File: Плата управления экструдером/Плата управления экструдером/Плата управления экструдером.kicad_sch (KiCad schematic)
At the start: 23 parts, among them J1 USB_C_Receptacle_USB2.0_16P, J2 Conn_01x02_Pin, J3 Conn_01x02_Pin, J4 Conn_01x02_Pin, U1 ATmega328P-A, U3 CH340N, Y1 Crystal

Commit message: Плата управления_обновл
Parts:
- added Q1, Q2, Q3, Q4, Q5: IRLB8721, Package_TO_SOT_THT:TO-220-3_Vertical, symbol Transistor_FET:Q_NMOS_GDS
- added bl_touch: Conn_01x05_Pin, symbol Connector:Conn_01x05_Pin
- added cooler_mod, cooler_mod1, fan, heater, switch, term: Conn_01x02_Pin, Connector_JST:JST_XH_B2B-XH-A_1x02_P2.50mm_Vertical, symbol Connector:Conn_01x02_Pin
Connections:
- net GND: now also Q1.3 (S), Q2.3 (S), Q3.3 (S), Q4.3 (S), Q5.3 (S)
- new net: Q5.2 (D), switch.2 (Pin_2)
- new net: Q3.2 (D), heater.2 (Pin_2)
- new net: Q1.2 (D), fan.2 (Pin_2)
- new net: cooler_mod.2 (Pin_2), cooler_mod1.1 (Pin_1)
- new net: Q4.2 (D), term.2 (Pin_2)
- new net +24V: Q2.2 (D), cooler_mod.1 (Pin_1), cooler_mod1.2 (Pin_2), fan.1 (Pin_1), heater.1 (Pin_1), switch.1 (Pin_1), term.1 (Pin_1)
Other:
- moved on the sheet: R3

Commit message: разводка платы
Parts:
- removed Q4, Q5: IRLB8721, Package_TO_SOT_THT:TO-220-3_Vertical, symbol Transistor_FET:Q_NMOS_GDS
- added C11: 0.1 uF, Capacitor_SMD:C_0805_2012Metric_Pad1.18x1.45mm_HandSolder, symbol Device:C
- added R4, R5, R6: 10k, Resistor_SMD:R_0805_2012Metric_Pad1.20x1.40mm_HandSolder, symbol Device:R
- added R7: 4.7k, Resistor_SMD:R_0805_2012Metric_Pad1.20x1.40mm_HandSolder, symbol Device:R
- C4: value 0.1 мкФ -> 0.1 uF
- renumbered POWER_IN_24V to POWER_IN_24V1, bl_touch to bl_touch1, cooler_mod to cooler_mod2, extruder to extruder1, fan to fan1, heater to heater1, switch to switch1, term to term1
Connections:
- net +24V: no longer switch1.1 (Pin_1), term1.1 (Pin_1)
- net +5V: now also bl_touch1.2 (Pin_2), R7.1
- net GND: now also bl_touch1.1 (Pin_1), bl_touch1.4 (Pin_4), switch1.2 (Pin_2), term1.2 (Pin_2), C11.2, R4.2, R5.2, R6.2
- net heater: now reaches Q3.1 (G)
- net heater: now also U1.26 (PC3), R6.1
- net fan_control: now reaches Q1.1 (G)
- net fan_control: now also U1.27 (PC4), R5.1
- net switch: now reaches U1.12 (PB0)
- net switch: now also switch1.1 (Pin_1)
- net BL_Z-min: now reaches U1.13 (PB1)
- net BL_Z-min: now also bl_touch1.5 (Pin_5)
- net termistor: now reaches U1.23 (PC0)
- net termistor: now also term1.1 (Pin_1), C11.1, R7.2
- net BL_contr_signal: now reaches U1.24 (PC1)
- net BL_contr_signal: now also bl_touch1.3 (Pin_3)
- net cooler: now reaches U1.28 (PC5)
- net cooler: now also Q2.1 (G), R4.1
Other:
- moved on the sheet: bl_touch1, switch1

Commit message: Плата управления раздел
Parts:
- added H1, H2, H3, H4: MountingHole, MountingHole:MountingHole_3.2mm_M3, symbol Mechanical:MountingHole
- Y1: footprint Crystal:Crystal_HC49-U_Vertical -> Crystal:Crystal_SMD_HC49-SD_HandSoldering

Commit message: Коннекторы
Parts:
- added J5, J6, J7, J8: Conn_01x08_Pin, Connector_PinSocket_2.54mm:PinSocket_1x08_P2.54mm_Vertical, symbol Connector:Conn_01x08_Pin
- Y1: footprint Crystal:Crystal_SMD_HC49-SD_HandSoldering -> Crystal:Crystal_HC49-4H_Vertical
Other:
- moved on the sheet: A1, C3, J2, J3, J4, POWER_IN_24V1, extruder1

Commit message: Правка платы
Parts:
- removed J2, J3, J4: Conn_01x02_Pin, symbol Connector:Conn_01x02_Pin
- removed cooler_mod2: Conn_01x02_Pin, Connector_JST:JST_XH_B2B-XH-A_1x02_P2.50mm_Vertical, symbol Connector:Conn_01x02_Pin
- added J9: Conn_02x03_Odd_Even, Connector_PinHeader_2.54mm:PinHeader_2x03_P2.54mm_Vertical, symbol Connector_Generic:Conn_02x03_Odd_Even
- J7, J8: footprint Connector_PinSocket_2.54mm:PinSocket_1x08_P2.54mm_Vertical -> Connector_PinHeader_2.54mm:PinHeader_1x08_P2.54mm_Vertical
- bl_touch1: footprint (none) -> Connector_JST:JST_XH_B5B-XH-A_1x05_P2.50mm_Vertical
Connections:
- net +24V: now also cooler_mod1.1 (Pin_1); no longer Q2.2 (D), cooler_mod1.2 (Pin_2)
- net +5V: now also J9.2 (Pin_2), J9.4 (Pin_4), J9.6 (Pin_6)
- net BL_Z-min: now also U1.23 (PC0); no longer U1.13 (PB1), bl_touch1.5 (Pin_5)
- net BL_contr_signal: no longer bl_touch1.3 (Pin_3)
- net GND: now also POWER_IN_24V1.1 (Pin_1); no longer POWER_IN_24V1.2 (Pin_2)
- net cooler: now also U1.27 (PC4); no longer Q2.1 (G), R4.1, U1.28 (PC5)
- net fan_control: now also U1.26 (PC3); no longer Q1.1 (G), R5.1, U1.27 (PC4)
- net heater: now also U1.25 (PC2); no longer Q3.1 (G), R6.1, U1.26 (PC3)
- net switch: now also U1.17 (PB5); no longer U1.12 (PB0), switch1.1 (Pin_1)
- net termistor: now also U1.19 (ADC6); no longer C11.1, R7.2, U1.23 (PC0), term1.1 (Pin_1)
- net STEP_PB: now reaches J7.1 (Pin_1)
- net STEP_PB: now also A1.15 (STEP)
- net ENABLE_PB: now reaches J7.2 (Pin_2)
- net ENABLE_PB: now also A1.9 (~{ENABLE})
- net DIR_PB: now reaches J7.3 (Pin_3)
- net DIR_PB: now also A1.16 (DIR)
- net at A1.12 (MS3): now also J9.5 (Pin_5)
- net STEP: now reaches J5.1 (Pin_1)
- net STEP: now also U1.32 (PD2)
- net DIR: now reaches J5.2 (Pin_2)
- net DIR: now also U1.1 (PD3)
- net ENABLE: now reaches J5.3 (Pin_3)
- net ENABLE: now also U1.2 (PD4)
- net BL_Z-min_PB: now reaches J8.1 (Pin_1)
- net BL_Z-min_PB: now also bl_touch1.5 (Pin_5)
- net BL_contr_signal_PB: now reaches J8.2 (Pin_2)
- net BL_contr_signal_PB: now also bl_touch1.3 (Pin_3)
- net fan_control_PB: now reaches J8.3 (Pin_3)
- net fan_control_PB: now also Q1.1 (G), R5.1
- net heater_PB: now reaches J8.4 (Pin_4)
- net heater_PB: now also Q3.1 (G), R6.1
- net cooler_PB: now reaches J8.5 (Pin_5)
- net cooler_PB: now also Q2.1 (G), R4.1
- net at A1.11 (MS2): now also J9.3 (Pin_3)
- net at A1.10 (MS1): now also J9.1 (Pin_1)
- net at A1.8 (VMOT), C3.1: now also POWER_IN_24V1.2 (Pin_2); no longer POWER_IN_24V1.1 (Pin_1)
- new net: Q2.2 (D), cooler_mod1.2 (Pin_2)
- new net switch_PB: switch1.1 (Pin_1)
- new net termistor_PB: C11.1, R7.2, term1.1 (Pin_1)
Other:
- moved on the sheet: J5, J7

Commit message: Начало трассировки
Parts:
- added J10: Conn_01x08_Pin, Connector_PinSocket_2.54mm:PinSocket_1x08_P2.54mm_Vertical, symbol Connector:Conn_01x08_Pin
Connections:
- net +5V: now also J5.1 (Pin_1), J7.1 (Pin_1)
- net BL_Z-min: now also J6.1 (Pin_1), U1.27 (PC4); no longer U1.23 (PC0)
- net BL_contr_signal: now also J6.2 (Pin_2), U1.26 (PC3); no longer U1.24 (PC1)
- net DIR: now also J5.7 (Pin_7), U1.2 (PD4); no longer J5.2 (Pin_2), U1.1 (PD3)
- net DIR_PB: now also J7.7 (Pin_7); no longer J7.3 (Pin_3)
- net ENABLE: now also J5.5 (Pin_5), U1.32 (PD2); no longer J5.3 (Pin_3), U1.2 (PD4)
- net ENABLE_PB: now also J7.5 (Pin_5); no longer J7.2 (Pin_2)
- net GND: now also J6.6 (Pin_6), J8.6 (Pin_6)
- net STEP: now also J5.6 (Pin_6), U1.1 (PD3); no longer J5.1 (Pin_1), U1.32 (PD2)
- net STEP_PB: now also J7.6 (Pin_6); no longer J7.1 (Pin_1)
- net cooler: now also J6.5 (Pin_5), U1.23 (PC0); no longer U1.27 (PC4)
- net fan_control: now also J6.3 (Pin_3), U1.25 (PC2); no longer U1.26 (PC3)
- net heater: now also J6.4 (Pin_4), U1.24 (PC1); no longer U1.25 (PC2)
- net switch: now also J6.8 (Pin_8)
- net switch_PB: now also J8.8 (Pin_8)
- net termistor: now also J6.7 (Pin_7)
- net termistor_PB: now also J8.7 (Pin_7)
- net PD6: now reaches U1.10 (PD6)
- net PD6: now also J10.2 (Pin_2)
- net PD7: now reaches U1.11 (PD7)
- net PD7: now also J10.3 (Pin_3)
- net PB0: now reaches U1.12 (PB0)
- net PB0: now also J10.4 (Pin_4)
- net PB1: now reaches U1.13 (PB1)
- net PB1: now also J10.5 (Pin_5)
- net PB2: now reaches U1.14 (PB2)
- net PB2: now also J10.6 (Pin_6)
- net PB3: now reaches U1.15 (PB3)
- net PB3: now also J10.7 (Pin_7)
- net PB4: now reaches U1.16 (PB4)
- net PB4: now also J10.8 (Pin_8)
- net PD5: now reaches U1.9 (PD5)
- net PD5: now also J10.1 (Pin_1)
- no-connect marks 2 -> 4

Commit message: Трассировка вечером
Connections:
- net +24V: now also A1.8 (VMOT), C3.1, POWER_IN_24V1.2 (Pin_2)
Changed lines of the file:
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@@
 	)
 	(junction
+		(at 304.8 113.03)
+		(diameter 0)
+		(color 0 0 0 0)
+	)
+	(junction
 		(at 199.39 78.74)
 		(diameter 0)
@@
 					(unit 1)
 				)
+			)
+		)
+	)
+	(symbol
+		(lib_id "power:+24V")
+		(at 304.8 113.03 0)
+		(unit 1)
+		(body_style 1)
+		(exclude_from_sim no)
+		(in_bom yes)
+		(on_board yes)
+		(in_pos_files yes)
+		(dnp no)
+		(fields_autoplaced yes)
+		(property "Reference" "#PWR034"
+			(at 304.8 116.84 0)
+			(hide yes)
+			(show_name no)
+			(do_not_autoplace no)
+			(effects
+				(font
+					(size 1.27 1.27)
+				)
+			)
+		)
+		(property "Value" "+24V"
+			(at 304.8 107.95 0)
+			(show_name no)
+			(do_not_autoplace no)
+			(effects
+				(font
+					(size 1.27 1.27)
+				)
+			)
+		)
+		(property "Footprint" ""
+			(at 304.8 113.03 0)
+			(hide yes)
+			(show_name no)
+			(do_not_autoplace no)
+			(effects
+				(font
+					(size 1.27 1.27)
+				)
+			)
+		)
+		(property "Datasheet" ""
+			(at 304.8 113.03 0)
+			(hide yes)
+			(show_name no)
+			(do_not_autoplace no)
+			(effects
+				(font
+					(size 1.27 1.27)
+				)
+			)
+		)
+		(property "Description" "Power symbol creates a global label with name \"+24V\""
+			(at 304.8 113.03 0)
+			(hide yes)
+			(show_name no)
+			(do_not_autoplace no)
+			(effects
+				(font
+					(size 1.27 1.27)
+				)
+			)
+		)
+		(pin "1"
+		)
+		(instances
+			(project "Плата управления экструдером"
+				(path "/b6ef5934-39d2-41a6-b7e8-7e2d7c9c4a1b"
+					(reference "#PWR034")
+					(unit 1)
+				)

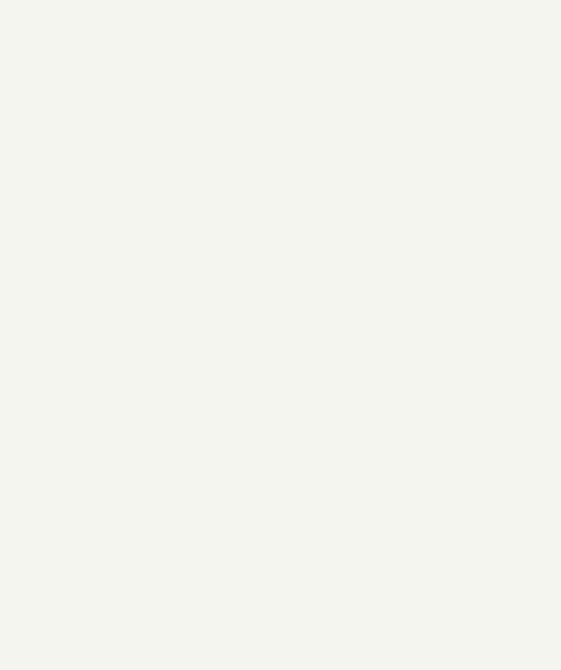
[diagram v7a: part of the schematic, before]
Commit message: Трассировка USB type C
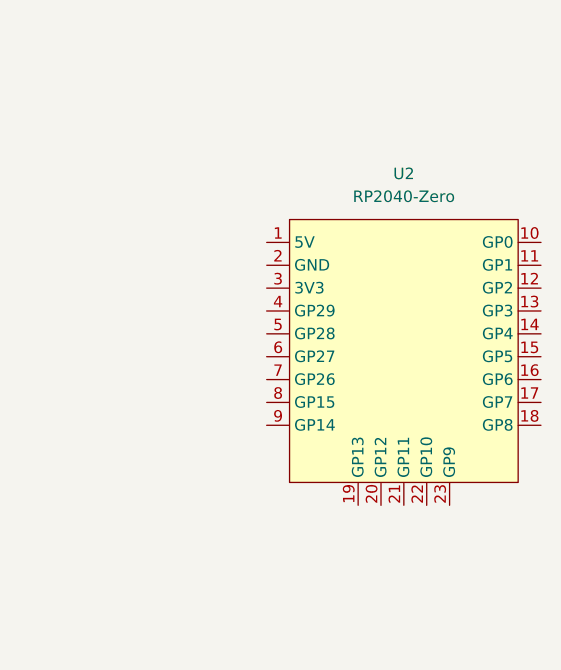
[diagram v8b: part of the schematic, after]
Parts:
- added U2: RP2040-Zero, symbol RP2040-Zero:RP2040-Zero
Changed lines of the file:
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@@
+	)
+	(symbol
+		(lib_id "RP2040-Zero:RP2040-Zero")
+		(at 477.52 59.69 0)
+		(unit 1)
+		(body_style 1)
+		(exclude_from_sim no)
+		(in_bom yes)
+		(on_board yes)
+		(in_pos_files yes)
+		(dnp no)
+		(fields_autoplaced yes)
+		(property "Reference" "U2"
+			(at 477.52 46.99 0)
+			(show_name no)
+			(do_not_autoplace no)
+			(effects
+				(font
+					(size 1.27 1.27)
+				)
+			)
+		)
+		(property "Value" "RP2040-Zero"
+			(at 477.52 49.53 0)
+			(show_name no)
+			(do_not_autoplace no)
+			(effects
+				(font
+					(size 1.27 1.27)
+				)
+			)
+		)
+		(property "Footprint" ""
+			(at 472.44 59.69 0)
+			(hide yes)
+			(show_name no)
+			(do_not_autoplace no)
+			(effects
+				(font
+					(size 1.27 1.27)
+				)
+			)
+		)
+		(property "Datasheet" ""
+			(at 472.44 59.69 0)
+			(hide yes)
+			(show_name no)
+			(do_not_autoplace no)
+			(effects
+				(font
+					(size 1.27 1.27)
+				)
+			)
+		)
+		(property "Description" ""
+			(at 477.52 59.69 0)
+			(hide yes)
+			(show_name no)
+			(do_not_autoplace no)
+			(effects
+				(font
+					(size 1.27 1.27)
+				)
+			)
+		)
+		(pin "1"
+		)
+		(pin "16"
+		)
+		(pin "18"
+		)
+		(pin "6"
+		)
+		(pin "15"
+		)
+		(pin "9"
+		)
+		(pin "17"
+		)
+		(pin "20"
+		)
+		(pin "8"
+		)
+		(pin "5"
+		)
+		(pin "19"
+		)
+		(pin "10"
+		)
+		(pin "14"
+		)
+		(pin "22"
+		)
+		(pin "7"
+		)
+		(pin "3"
+		)
+		(pin "11"
+		)
+		(pin "4"
+		)
+		(pin "13"
+		)
+		(pin "2"
+		)
+		(pin "12"
+		)
+		(pin "21"
+		)
+		(pin "23"
+		)
+		(instances
+			(project "Плата управления экструдером"
+				(path "/b6ef5934-39d2-41a6-b7e8-7e2d7c9c4a1b"
+					(reference "U2")
+					(unit 1)
+				)
+			)
+		)
 	)
 	(symbol
